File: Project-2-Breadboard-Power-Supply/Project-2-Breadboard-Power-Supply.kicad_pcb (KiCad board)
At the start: 2 copper layers, 16 parts, among them J1 Conn_01x02_Pin, J2 Conn_01x02_Pin, J3 Conn_01x03_Pin, J4 Conn_01x03_Pin, J5 Screw_Terminal_01x02, J6 Barrel_Jack_Switch, J7 Screw_Terminal_01x02, U1 LM7805_TO220, U2 LM317_TO-220

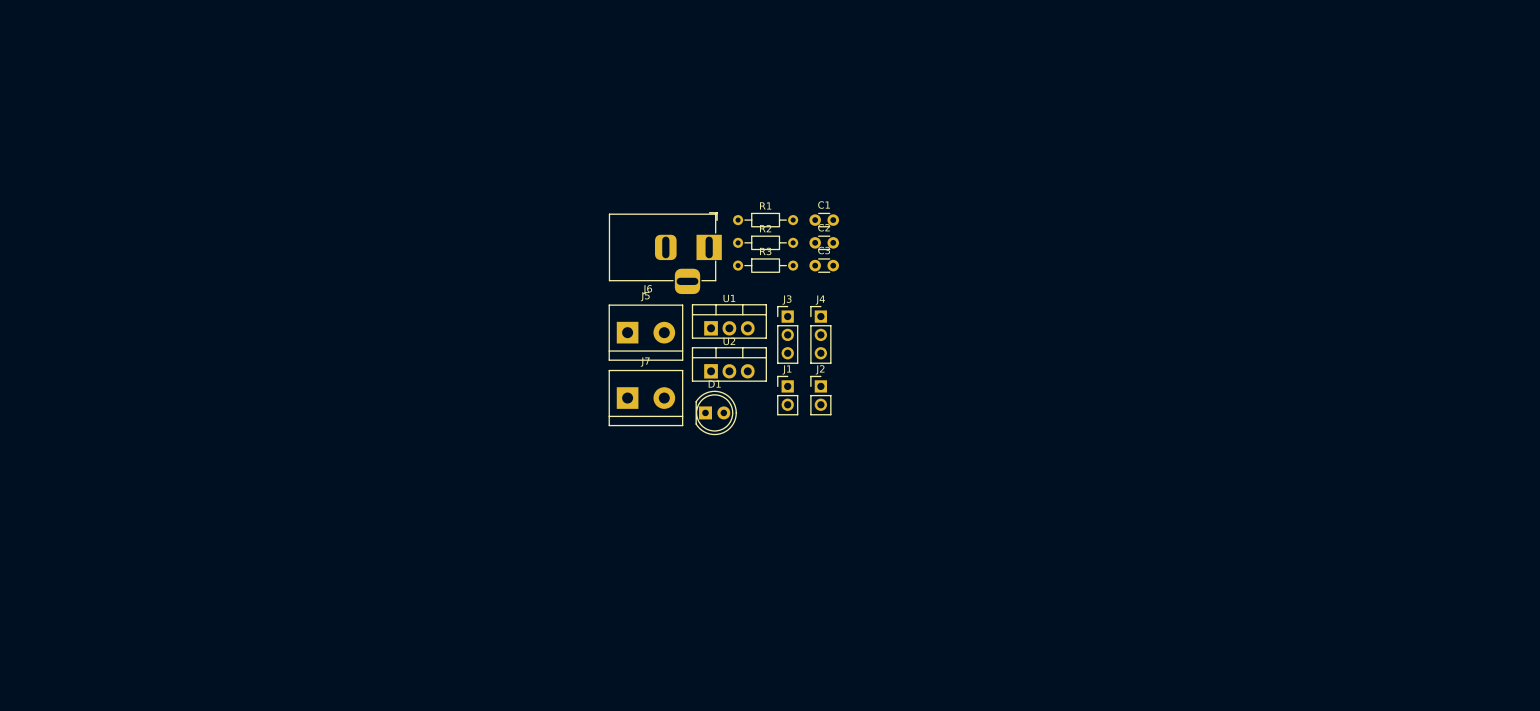
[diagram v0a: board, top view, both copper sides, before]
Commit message: place and lock connectors J1, J2
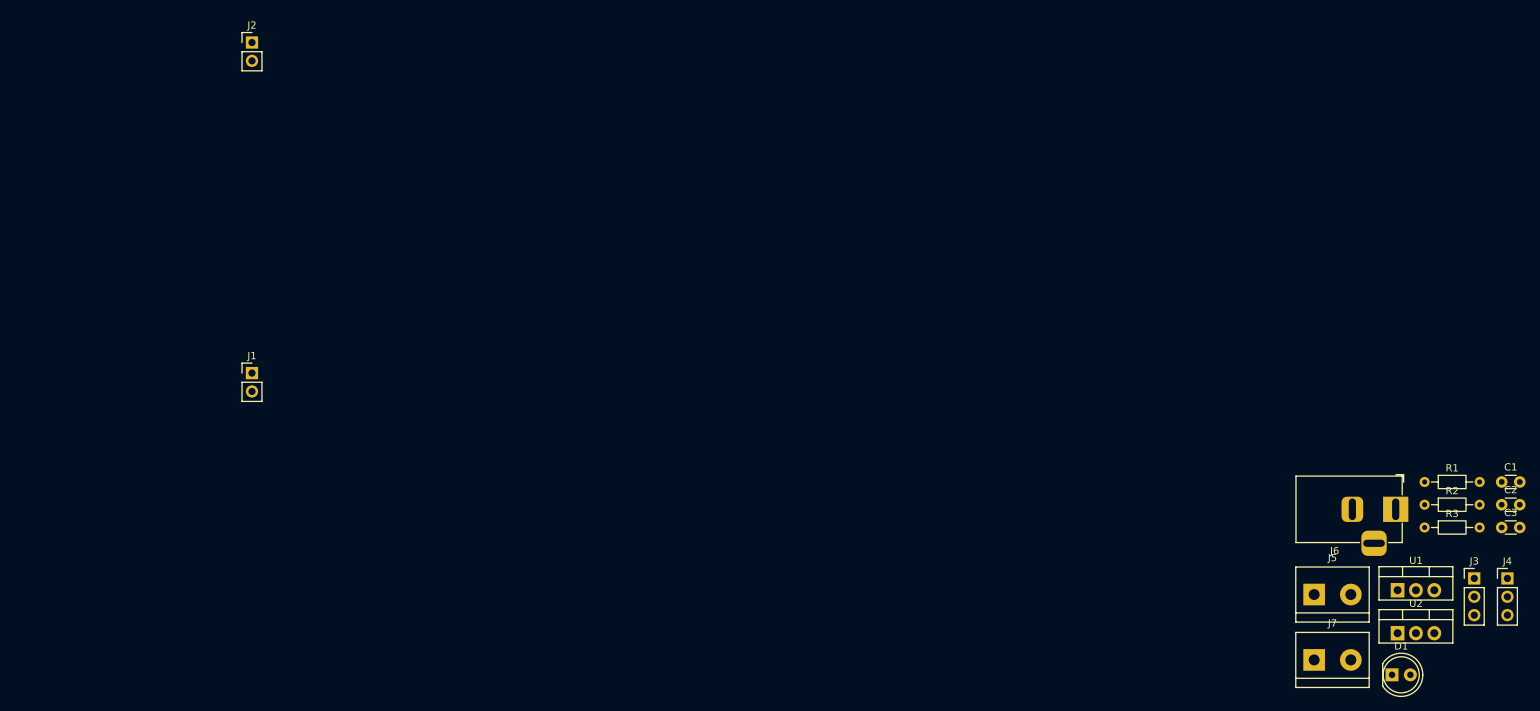
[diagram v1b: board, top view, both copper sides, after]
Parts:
- moved C1 101.7 mm to (234.0, 108.3)
- moved C2 101.7 mm to (234.0, 111.5)
- moved C3 101.7 mm to (234.0, 114.6)
- moved U1 101.7 mm to (219.6, 123.3)
- moved U2 101.7 mm to (219.6, 129.2)
- moved D1 101.7 mm to (218.8, 135.0)
- moved J5 101.7 mm to (208.0, 123.9)
- moved J7 101.7 mm to (208.0, 132.9)
- moved J3 101.7 mm to (230.2, 121.7)
- moved J4 101.7 mm to (234.8, 121.7)
- moved J6 101.7 mm to (219.3, 112.1)
- moved R1 101.7 mm to (223.3, 108.3)
- moved R2 101.7 mm to (223.3, 111.5)
- moved R3 101.7 mm to (223.3, 114.6)
- moved J2 92.0 mm to (61.0, 47.5)
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
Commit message: place and lock scre terminals J5, J7
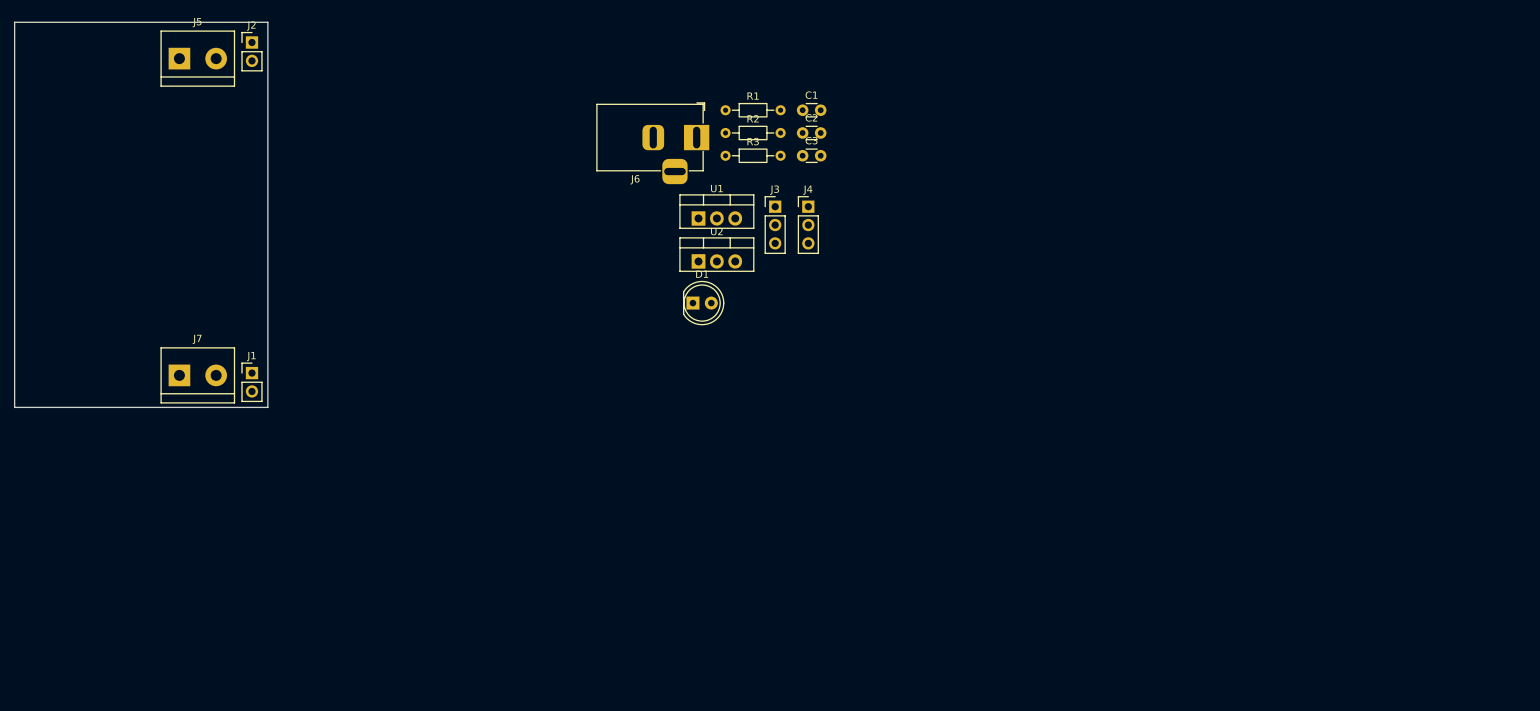
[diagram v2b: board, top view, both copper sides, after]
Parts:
- moved J5 173.7 mm to (51.0, 49.7)
- moved J7 161.9 mm to (51.0, 93.6)
- moved C3 109.6 mm to (137.2, 63.2)
- moved J3 109.6 mm to (133.4, 70.2)
- moved J4 109.6 mm to (138.0, 70.2)
- moved J6 109.6 mm to (122.5, 60.7)
- moved R1 109.6 mm to (126.5, 56.9)
- moved R2 109.6 mm to (126.5, 60.0)
- moved R3 109.6 mm to (126.5, 63.2)
- moved U1 109.6 mm to (122.8, 71.8)
- moved U2 109.6 mm to (122.8, 77.8)
- moved C1 109.6 mm to (137.2, 56.9)
- moved C2 109.6 mm to (137.2, 60.0)
- moved D1 109.6 mm to (122.0, 83.6)
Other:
- board outline added: 35.1 x 53.3 mm
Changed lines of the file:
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@@
 	(footprint "Resistor_THT:R_Axial_DIN0204_L3.6mm_D1.6mm_P7.62mm_Horizontal"
 		(layer "F.Cu")
-		(at 223.29 114.62)
+		(at 126.54 63.17)
 		(descr "Resistor, Axial_DIN0204 series, Axial, Horizontal, pin pitch=7.62mm, 0.167W, length*diameter=3.6*1.6mm^2, http://cdn-reichelt.de/documents/datenblatt/B400/1_4W%23YAG.pdf")
 		(tags "Resistor Axial_DIN0204 series Axial Horizontal pin pitch 7.62mm 0.167W length 3.6mm diameter 1.6mm")
@@
 	)
 	(footprint "TerminalBlock:TerminalBlock_bornier-2_P5.08mm"
+		(locked yes)
 		(layer "F.Cu")
-		(at 208 132.95)
+		(at 50.96 93.57)
 		(descr "simple 2-pin terminal block, pitch 5.08mm, revamped version of bornier2")
 		(tags "terminal block bornier2")
@@
 	(footprint "Connector_PinHeader_2.54mm:PinHeader_1x03_P2.54mm_Vertical"
 		(layer "F.Cu")
-		(at 234.75 121.67)
+		(at 138 70.22)
 		(descr "Through hole straight pin header, 1x03, 2.54mm pitch, single row")
 		(tags "Through hole pin header THT 1x03 2.54mm single row")
@@
 	(footprint "Capacitor_THT:C_Disc_D3.0mm_W1.6mm_P2.50mm"
 		(layer "F.Cu")
-		(at 233.96 111.47)
+		(at 137.21 60.02)
 		(descr "C, Disc series, Radial, pin pitch=2.50mm, diameter*width=3.0*1.6mm^2, Capacitor, http://www.vishay.com/docs/45233/krseries.pdf")
 		(tags "C Disc series Radial pin pitch 2.50mm diameter 3.0mm width 1.6mm Capacitor")
@@
 	(footprint "LED_THT:LED_D5.0mm"
 		(layer "F.Cu")
-		(at 218.78 135.01)
+		(at 122.03 83.56)
 		(descr "LED, diameter 5.0mm, 2 pins, http://cdn-reichelt.de/documents/datenblatt/A500/LL-504BC2E-009.pdf, generated by kicad-footprint-generator")
 		(tags "LED")
@@
 		)
 		(point
-			(at 220.05 135.01)
+			(at 123.3 83.56)
 			(size 2)
 			(layer "F.Fab")
@@
 	(footprint "Connector_PinHeader_2.54mm:PinHeader_1x03_P2.54mm_Vertical"
 		(layer "F.Cu")
-		(at 230.16 121.67)
+		(at 133.41 70.22)
 		(descr "Through hole straight pin header, 1x03, 2.54mm pitch, single row")
 		(tags "Through hole pin header THT 1x03 2.54mm single row")
@@
 	)
 	(footprint "TerminalBlock:TerminalBlock_bornier-2_P5.08mm"
+		(locked yes)
 		(layer "F.Cu")
-		(at 208 123.9)
+		(at 50.96 49.73)
 		(descr "simple 2-pin terminal block, pitch 5.08mm, revamped version of bornier2")
 		(tags "terminal block bornier2")
@@
 	(footprint "Resistor_THT:R_Axial_DIN0204_L3.6mm_D1.6mm_P7.62mm_Horizontal"
 		(layer "F.Cu")
-		(at 223.29 111.47)
+		(at 126.54 60.02)
 		(descr "Resistor, Axial_DIN0204 series, Axial, Horizontal, pin pitch=7.62mm, 0.167W, length*diameter=3.6*1.6mm^2, http://cdn-reichelt.de/documents/datenblatt/B400/1_4W%23YAG.pdf")
 		(tags "Resistor Axial_DIN0204 series Axial Horizontal pin pitch 7.62mm 0.167W length 3.6mm diameter 1.6mm")
@@
 	(footprint "Capacitor_THT:C_Disc_D3.0mm_W1.6mm_P2.50mm"
 		(layer "F.Cu")
-		(at 233.96 114.62)
+		(at 137.21 63.17)
 		(descr "C, Disc series, Radial, pin pitch=2.50mm, diameter*width=3.0*1.6mm^2, Capacitor, http://www.vishay.com/docs/45233/krseries.pdf")
 		(tags "C Disc series Radial pin pitch 2.50mm diameter 3.0mm width 1.6mm Capacitor")
@@
 	(footprint "Resistor_THT:R_Axial_DIN0204_L3.6mm_D1.6mm_P7.62mm_Horizontal"
 		(layer "F.Cu")
-		(at 223.29 108.32)
+		(at 126.54 56.87)
 		(descr "Resistor, Axial_DIN0204 series, Axial, Horizontal, pin pitch=7.62mm, 0.167W, length*diameter=3.6*1.6mm^2, http://cdn-reichelt.de/documents/datenblatt/B400/1_4W%23YAG.pdf")
 		(tags "Resistor Axial_DIN0204 series Axial Horizontal pin pitch 7.62mm 0.167W length 3.6mm diameter 1.6mm")
@@
 	(footprint "Package_TO_SOT_THT:TO-220-3_Vertical"
 		(layer "F.Cu")
-		(at 219.55 129.25)
+		(at 122.8 77.8)
 		(descr "TO-220-3, Vertical, RM 2.54mm, see https://www.vishay.com/docs/66542/to-220-1.pdf")
 		(tags "TO-220-3 Vertical RM 2.54mm")
@@
 	(footprint "Connector_BarrelJack:BarrelJack_Horizontal"
 		(layer "F.Cu")
-		(at 219.29 112.105)
+		(at 122.54 60.655)
 		(descr "DC Barrel Jack")
 		(tags "Power Jack")
@@
 	(footprint "Capacitor_THT:C_Disc_D3.0mm_W1.6mm_P2.50mm"
 		(layer "F.Cu")
-		(at 233.96 108.32)
+		(at 137.21 56.87)
 		(descr "C, Disc series, Radial, pin pitch=2.50mm, diameter*width=3.0*1.6mm^2, Capacitor, http://www.vishay.com/docs/45233/krseries.pdf")
 		(tags "C Disc series Radial pin pitch 2.50mm diameter 3.0mm width 1.6mm Capacitor")
@@
 	(footprint "Package_TO_SOT_THT:TO-220-3_Vertical"
 		(layer "F.Cu")
-		(at 219.55 123.3)
+		(at 122.8 71.85)
 		(descr "TO-220-3, Vertical, RM 2.54mm, see https://www.vishay.com/docs/66542/to-220-1.pdf")
 		(tags "TO-220-3 Vertical RM 2.54mm")
@@
 		)
 	)
+	(gr_rect
+		(start 28.15 44.7)
+		(end 63.2 98)
+		(stroke
+			(width 0.05)
+			(type default)
+		)
+		(fill no)
+		(layer "Edge.Cuts")
+	)
 	(embedded_fonts no)
